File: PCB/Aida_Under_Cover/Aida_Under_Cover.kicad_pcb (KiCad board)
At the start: 2 copper layers, 119.7 x 83.3 mm, 15 parts

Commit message: 原点ガイドを追加。基板Mid_InsideのLED穴形状調整
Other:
- board text added: "Center Origin"
- board text added: "Grid Origin"
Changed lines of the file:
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@@
 		(layer "Edge.Cuts")
+	)
+	(gr_circle
+		(center 152.4 23.8125)
+		(end 153.590625 23.8125)
+		(stroke
+			(width 0.1)
+			(type default)
+		)
+		(fill no)
+		(layer "User.1")
+	)
+	(gr_line
+		(start 21.43125 23.8125)
+		(end 26.19375 23.8125)
+		(stroke
+			(width 0.1)
+			(type default)
+		)
+		(layer "User.1")
+	)
+	(gr_circle
+		(center 23.8125 23.8125)
+		(end 25.003125 23.8125)
+		(stroke
+			(width 0.1)
+			(type default)
+		)
+		(fill no)
+		(layer "User.1")
+	)
+	(gr_line
+		(start 23.8125 21.43125)
+		(end 23.8125 26.19375)
+		(stroke
+			(width 0.1)
+			(type default)
+		)
+		(layer "User.1")
+	)
+	(gr_line
+		(start 150.01875 23.8125)
+		(end 154.78125 23.8125)
+		(stroke
+			(width 0.1)
+			(type default)
+		)
+		(layer "User.1")
+	)
+	(gr_line
+		(start 152.4 21.43125)
+		(end 152.4 26.19375)
+		(stroke
+			(width 0.1)
+			(type default)
+		)
+		(layer "User.1")
 	)
 	(gr_text "Top PCB outline"
@@
 		(at 42.267197 32.1469 0)
 		(layer "Eco2.User")
+		(effects
+			(font
+				(size 1 1)
+				(thickness 0.15)
+			)
+			(justify left bottom)
+		)
+	)
+	(gr_text "Center Origin"
+		(at 148.828125 21.43125 0)
+		(layer "User.1")
+		(effects
+			(font
+				(size 1 1)
+				(thickness 0.15)
+			)
+			(justify left bottom)
+		)
+	)
+	(gr_text "Grid Origin"
+		(at 20.240625 21.43125 0)
+		(layer "User.1")
 		(effects
 			(font
@@
 		)
 	)
+	(group ""
+		(members "065d6681-7ba5-4588-98c6-80817ce4f8f7" "0c8be5e7-ea1f-4f6a-b85c-1cfcafa569f7"
+			"ecfa8c62-a0ef-4eca-aafe-9966ff6fbb19" "f9cb1e02-b91f-48ec-8bfa-2dcedd4acf70"
+		)
+	)
+	(group ""
+		(members "372d44a1-f9fd-42d5-bfe7-77f223b9e496" "56a9333c-898b-4629-9a27-55d00b1f2ede"
+			"e650641b-a698-4586-9d26-6d65606f35b7" "ecb66218-12f0-4505-a5dc-e84e84e1582e"
+		)
+	)

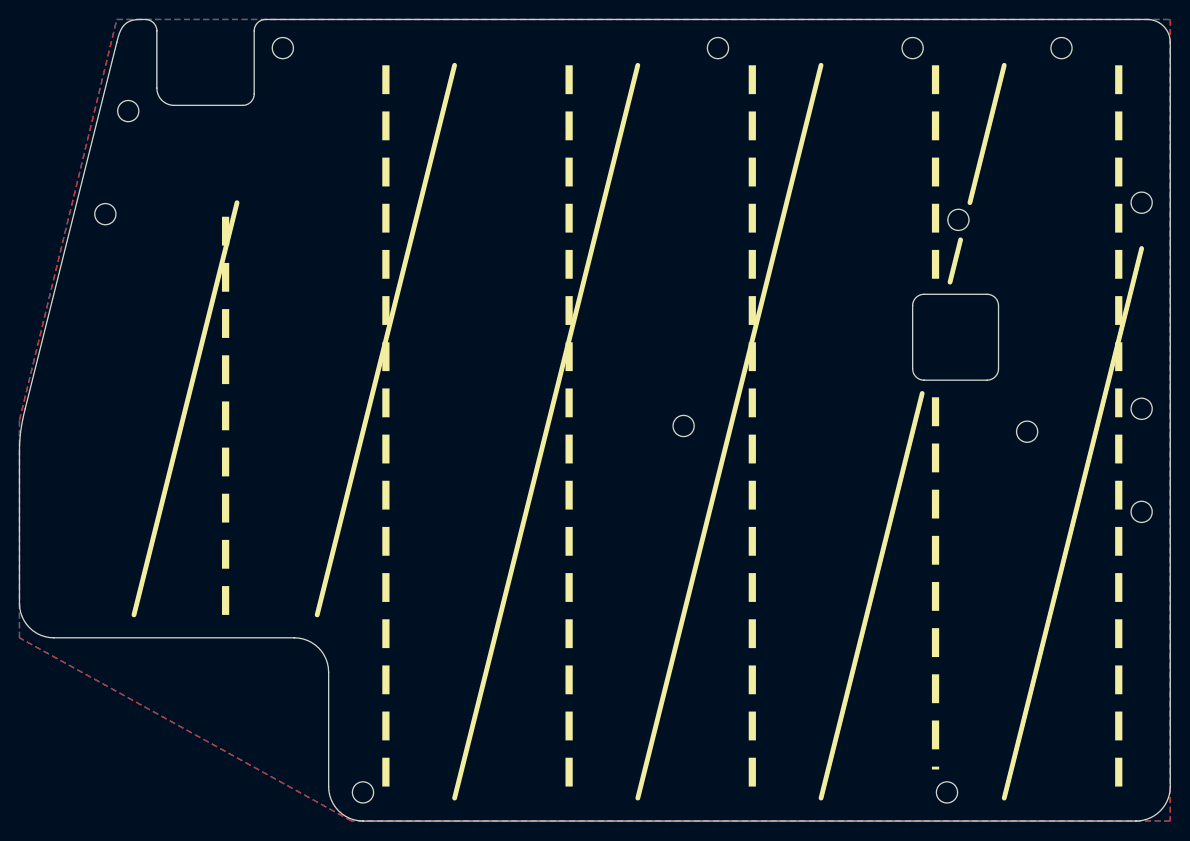
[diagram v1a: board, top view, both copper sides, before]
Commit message: 開発ナンバーと表裏を記載
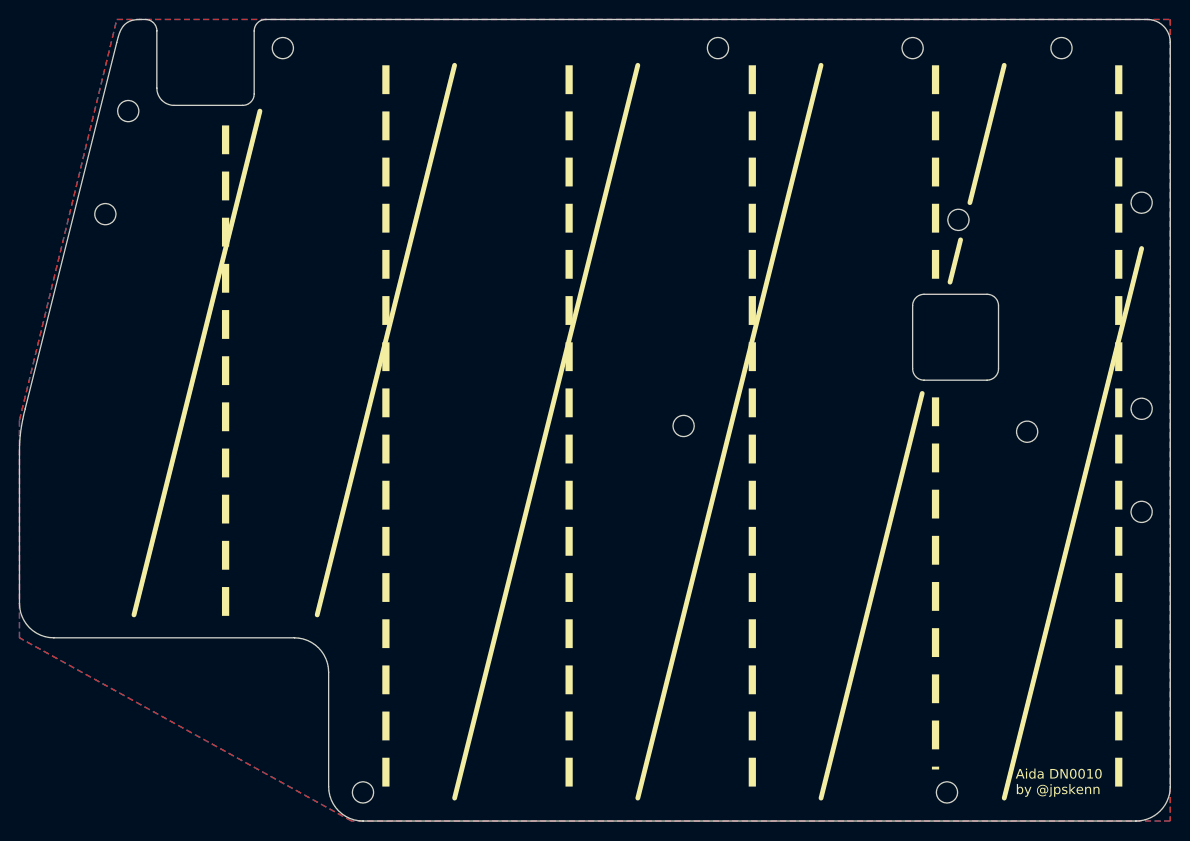
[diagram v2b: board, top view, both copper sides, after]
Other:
- board text added: "Aida DN0010 by @jpskenn"
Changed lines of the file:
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@@
 	)
 	(gr_line
-		(start 52.38756 53.850024)
-		(end 52.387524 96.7125)
+		(start 52.3869 44.35035)
+		(end 52.386864 97.009725)
 		(stroke
 			(width 0.75)
@@
 	)
 	(gr_line
-		(start 53.578125 52.3875)
+		(start 55.959375 42.8625)
 		(end 42.8625 95.25)
 		(stroke
@@
 	)
 	(gr_line
-		(start 53.57815 52.387524)
+		(start 55.959375 42.8625)
 		(end 42.862525 95.250024)
 		(stroke
@@
 	)
 	(gr_line
-		(start 52.38756 53.850024)
-		(end 52.387524 96.7125)
+		(start 52.38756 44.35035)
+		(end 52.387524 97.009725)
 		(stroke
 			(width 0.75)
@@
 		(layer "User.1")
 	)
+	(gr_text "Aida DN0010\nby @jpskenn"
+		(at 134.5383 114.00045 0)
+		(layer "F.SilkS")
+		(effects
+			(font
+				(size 1 1)
+				(thickness 0.1)
+			)
+			(justify left bottom)
+		)
+	)
+	(gr_text "Aida DN0010\nby @jpskenn"
+		(at 144.6584 114.00045 0)
+		(layer "B.SilkS")
+		(effects
+			(font
+				(size 1 1)
+				(thickness 0.1)
+			)
+			(justify left bottom mirror)
+		)
+	)
 	(gr_text "Top PCB outline"

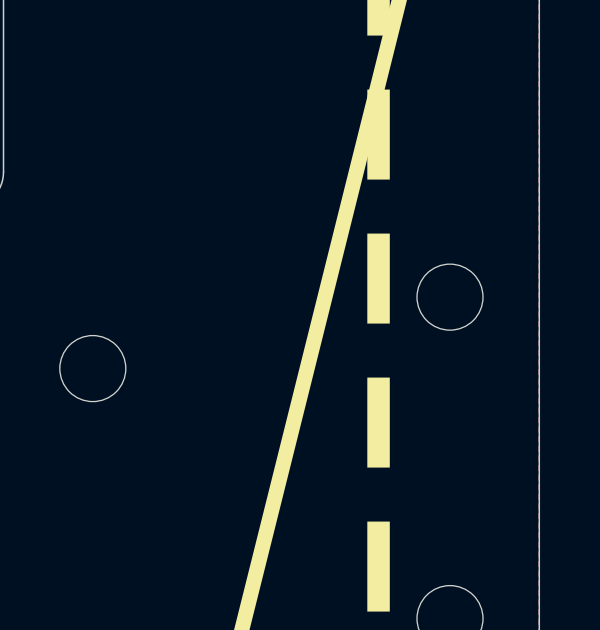
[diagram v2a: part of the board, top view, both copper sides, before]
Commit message: LEDを1/16u下へ移動。 右手のフラッシュメモリとの干渉回避のためボトムプレートの穴位置調整。
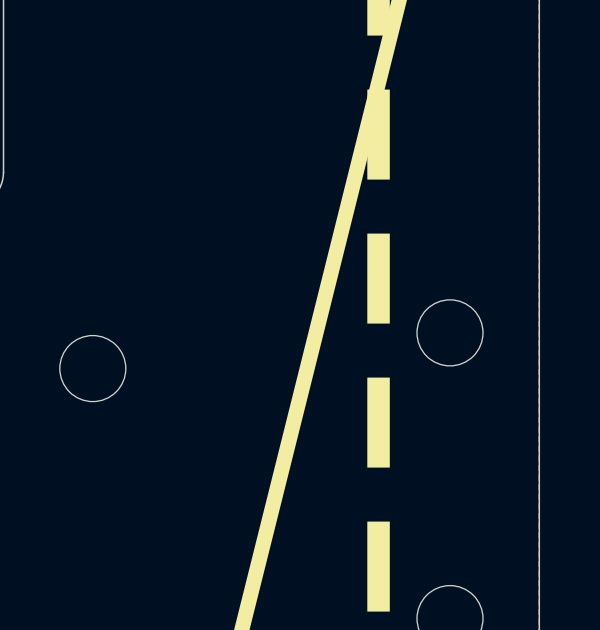
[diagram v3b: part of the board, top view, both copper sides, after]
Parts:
- moved REF** 1.19 mm to (147.6, 75.0)
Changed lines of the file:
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@@
 	(footprint "MountingHole:MountingHole_2.2mm_M2"
 		(layer "F.Cu")
-		(at 147.637604 73.818792)
+		(at 147.6375 75.009375)
 		(descr "Mounting Hole 2.2mm, M2, no annular, generated by kicad-footprint-generator mountinghole.py")
 		(tags "mountinghole M2")
